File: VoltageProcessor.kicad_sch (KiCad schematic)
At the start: 29 parts, among them J1 PJ301M-12, J2 PJ301M-12, J3 Eurorack power, J3 PJ301M-12, J4 PJ301M-12, U1 TL074

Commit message: IO Placement
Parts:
- renumbered J3 to J5
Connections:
- net at R1.1: now also RV1.2
- net at RV2.2: now also R2.1
- no-connect marks 8 -> 4
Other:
- moved on the sheet: J1, J2, RV1, RV2

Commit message: Pre route
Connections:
- net GND: no longer U1.6 (-)
- net at R4.2, R6.1, R9.1: now also U1.1; no longer U1.7
- net at R1.2, R3.1: now also U1.5 (+); no longer U1.2 (-)
- net at R3.2, R5.1, R8.1: now also U1.7; no longer U1.1
- net at R2.2, R4.1: now also U1.2 (-); no longer U1.5 (+)

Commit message: Add silkscreen text, and last DRC issues
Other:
- company: (none) -> joppeboeve.nl
- title: (none) -> Voltage Processor
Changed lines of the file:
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@@
 	(generator_version "8.0")
 	(paper "A4")
+	(title_block
+		(title "Voltage Processor")
+		(date "2024-07-28")
+		(rev "0.1")
+		(company "joppeboeve.nl")
+	)
 	(junction
 		(at 113.03 177.8)

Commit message: Connected input CV jack's switch to GND instead of NC Add schematic picture
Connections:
- net GND: now also J1.2, J2.2
- no-connect marks 4 -> 2
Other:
- note removed: "NOTE: Maybe ground jacks instead of NC?"
- moved on the sheet: C1, C2, C3, C4, C5, C6, J1, J2, J3, J4, J5, R1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

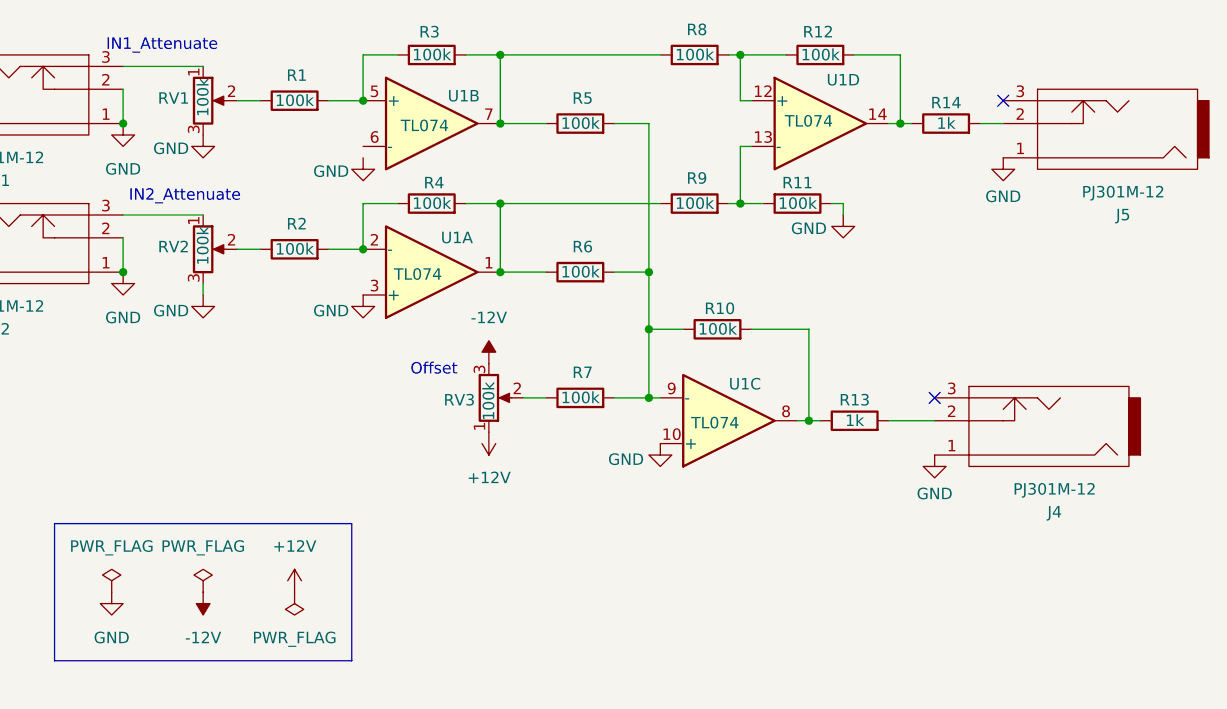
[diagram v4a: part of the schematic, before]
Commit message: Swapped `U1B` inputs to match that of `U1A`, so that it does work
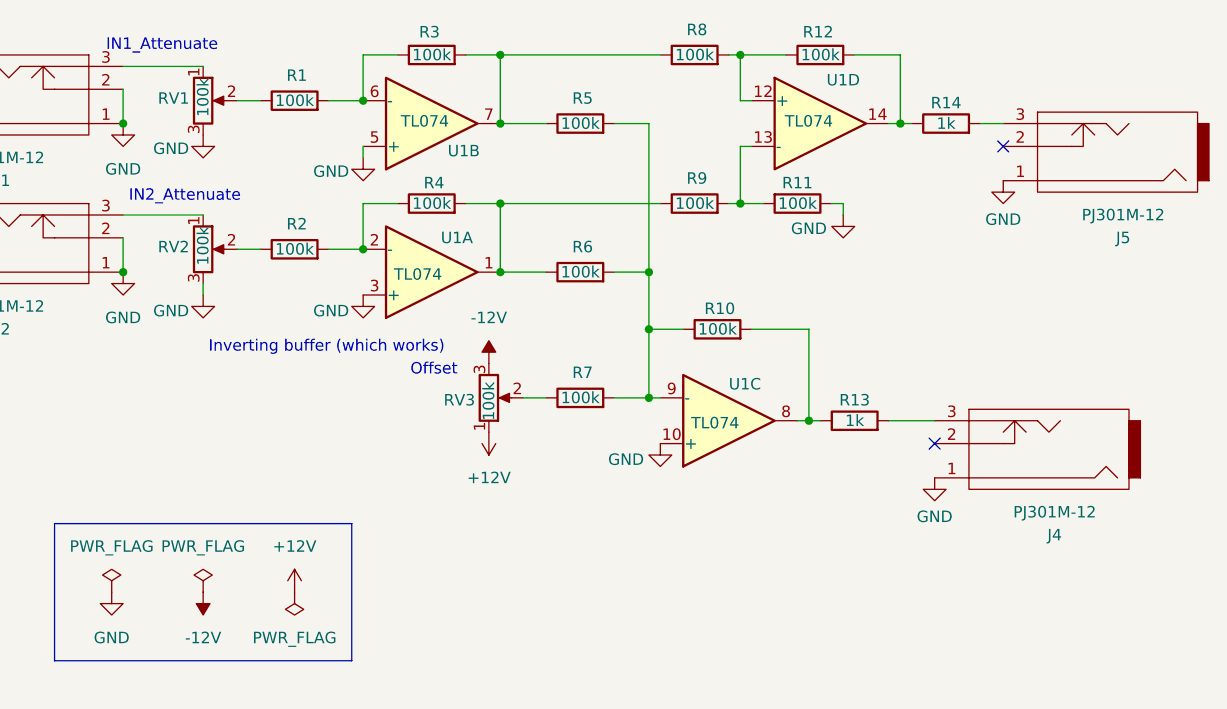
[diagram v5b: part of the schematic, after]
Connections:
- net GND: now also U1.5 (+)
- net at J4.2: no longer R13.2
- net at J4.3: now also R13.2
- net at R1.2, R3.1: now also U1.6 (-); no longer U1.5 (+)
- net at J5.2: no longer R14.2
- net at J5.3: now also R14.2
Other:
- note added: "Inverting buffer (which works)"
- moved on the sheet: J4, J5
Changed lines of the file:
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@@
 	)
 	(no_connect
-		(at 167.64 35.56)
+		(at 160.02 73.66)
 	)
 	(no_connect
-		(at 160.02 68.58)
+		(at 167.64 40.64)
 	)
 	(wire
@@
 	(wire
 		(pts
-			(xy 154.94 71.12) (xy 160.02 71.12)
-		)
-		(stroke
-			(width 0)
-			(type default)
-		)
-	)
-	(wire
-		(pts
 			(xy 138.43 40.64) (xy 138.43 46.99)
 		)
@@
 	(wire
 		(pts
-			(xy 111.76 54.61) (xy 116.84 54.61)
+			(xy 154.94 71.12) (xy 160.02 71.12)
 		)
 		(stroke
@@
 	(wire
 		(pts
-			(xy 114.3 68.58) (xy 116.84 68.58)
+			(xy 111.76 54.61) (xy 116.84 54.61)
 		)
 		(stroke
@@
 		)
 	)
-	(polyline
+	(wire
 		(pts
-			(xy 62.23 82.55) (xy 95.25 82.55)
+			(xy 114.3 68.58) (xy 116.84 68.58)
 		)
 		(stroke
@@
 		)
 	)
-	(wire
+	(polyline
 		(pts
-			(xy 165.1 38.1) (xy 167.64 38.1)
+			(xy 62.23 82.55) (xy 95.25 82.55)
 		)
 		(stroke
@@
 	(wire
 		(pts
+			(xy 96.52 40.64) (xy 96.52 41.91)
+		)
+		(stroke
+			(width 0)
+			(type default)
+		)
+	)
+	(wire
+		(pts
 			(xy 128.27 54.61) (xy 128.27 60.96)
 		)
@@
 	(wire
 		(pts
+			(xy 165.1 38.1) (xy 167.64 38.1)
+		)
+		(stroke
+			(width 0)
+			(type default)
+		)
+	)
+	(wire
+		(pts
 			(xy 36.83 83.82) (xy 34.29 83.82)
 		)
@@
 		)
 	)
+	(text "Inverting buffer (which works)"
+		(exclude_from_sim no)
+		(at 92.456 62.992 0)
+		(effects
+			(font
+				(size 1.27 1.27)
+			)
+		)
+	)
 	(text "IN2_Attenuate"
 		(exclude_from_sim no)
@@
 	(symbol
 		(lib_id "eurocad:PJ301M-12")
-		(at 171.45 71.12 180)
+		(at 171.45 73.66 180)
 		(unit 1)
 		(exclude_from_sim no)
@@
 		(dnp no)
 		(property "Reference" "J4"
-			(at 173.355 81.28 0)
+			(at 173.355 83.82 0)
 			(effects
 				(font
@@
 		)
 		(property "Value" "PJ301M-12"
-			(at 173.355 78.74 0)
+			(at 173.355 81.28 0)
 			(effects
 				(font
@@
 		)
 		(property "Footprint" "Eurocad:PJ301M-12"
-			(at 171.45 71.12 0)
+			(at 171.45 73.66 0)
 			(effects
 				(font
@@
 		)
 		(property "Datasheet" ""
-			(at 171.45 71.12 0)
+			(at 171.45 73.66 0)
 			(effects
 				(font
@@
 		)
 		(property "Description" ""
-			(at 171.45 71.12 0)
+			(at 171.45 73.66 0)
 			(effects
 				(font
@@
 	(symbol
 		(lib_id "eurocad:PJ301M-12")
-		(at 179.07 38.1 180)
+		(at 179.07 40.64 180)
 		(unit 1)
 		(exclude_from_sim no)
@@
 		(dnp no)
 		(property "Reference" "J5"
-			(at 180.975 48.26 0)
+			(at 180.975 50.8 0)
 			(effects
 				(font
@@
 		)
 		(property "Value" "PJ301M-12"
-			(at 180.975 45.72 0)
+			(at 180.975 48.26 0)
 			(effects
 				(font
@@
 		)
 		(property "Footprint" "Eurocad:PJ301M-12"
-			(at 179.07 38.1 0)
+			(at 179.07 40.64 0)
 			(effects
 				(font
@@
 		)
 		(property "Datasheet" ""
-			(at 179.07 38.1 0)
+			(at 179.07 40.64 0)
 			(effects
 				(font
@@
 		)
 		(property "Description" ""
-			(at 179.07 38.1 0)
+			(at 179.07 40.64 0)
 			(effects
 				(font
@@
 	(symbol
 		(lib_id "power:GND")
-		(at 167.64 41.91 0)
+		(at 167.64 44.45 0)
 		(unit 1)
 		(exclude_from_sim no)
@@
 		(dnp no)
 		(property "Reference" "#PWR024"
-			(at 167.64 48.26 0)
+			(at 167.64 50.8 0)
 			(effects
 				(font
@@
 		)
 		(property "Value" "GND"
-			(at 167.64 46.228 0)
+			(at 167.64 48.768 0)
 			(effects
 				(font
@@
 		)
 		(property "Footprint" ""
-			(at 167.64 41.91 0)
+			(at 167.64 44.45 0)
 			(effects
 				(font
@@
 		)
 		(property "Datasheet" ""
-			(at 167.64 41.91 0)
+			(at 167.64 44.45 0)
 			(effects
 				(font
@@
 		)
 		(property "Description" "Power symbol creates a global label with name \"GND\" , ground"
-			(at 167.64 41.91 0)
+			(at 167.64 44.45 0)
 			(effects
 				(font
@@
 		(lib_id "Amplifier_Operational:TL074")
 		(at 104.14 38.1 0)
+		(mirror x)
 		(unit 2)
 		(exclude_from_sim no)
@@
 		(dnp no)
 		(property "Reference" "U1"
-			(at 107.696 35.052 0)
+			(at 107.696 41.148 0)
 			(effects
 				(font
@@
 		)
 		(property "Value" "TL074"
-			(at 103.378 38.354 0)
+			(at 103.378 37.846 0)
 			(effects
 				(font
@@
 		)
 		(property "Footprint" "Package_DIP:DIP-14_W7.62mm"
-			(at 102.87 35.56 0)
+			(at 102.87 40.64 0)
 			(effects
 				(font
@@
 		)
 		(property "Datasheet" "http://www.ti.com/lit/ds/symlink/tl071.pdf"
-			(at 105.41 33.02 0)
+			(at 105.41 43.18 0)
 			(effects
 				(font
@@
 	(symbol
 		(lib_id "power:GND")
-		(at 160.02 74.93 0)
+		(at 160.02 77.47 0)
 		(unit 1)
 		(exclude_from_sim no)
@@
 		(dnp no)
 		(property "Reference" "#PWR023"
-			(at 160.02 81.28 0)
+			(at 160.02 83.82 0)
 			(effects
 				(font
@@
 		)
 		(property "Value" "GND"
-			(at 160.02 79.248 0)
+			(at 160.02 81.788 0)
 			(effects
 				(font
@@
 		)
 		(property "Footprint" ""
-			(at 160.02 74.93 0)
+			(at 160.02 77.47 0)
 			(effects
 				(font
@@
 		)
 		(property "Datasheet" ""
-			(at 160.02 74.93 0)
+			(at 160.02 77.47 0)
 			(effects
 				(font
@@
 		)
 		(property "Description" "Power symbol creates a global label with name \"GND\" , ground"
-			(at 160.02 74.93 0)
+			(at 160.02 77.47 0)
 			(effects
 				(font

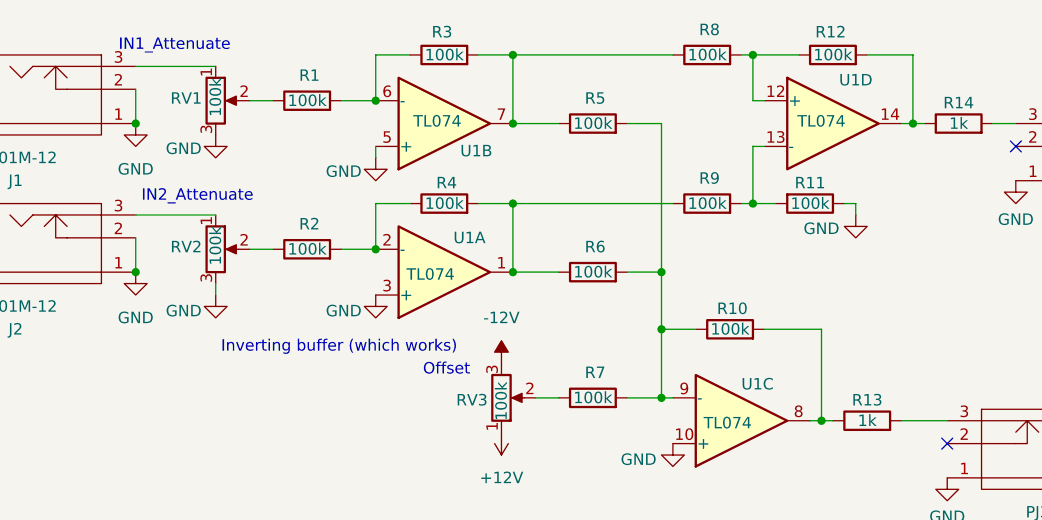
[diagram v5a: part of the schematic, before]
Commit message: Switched `RV1` and `RV2`
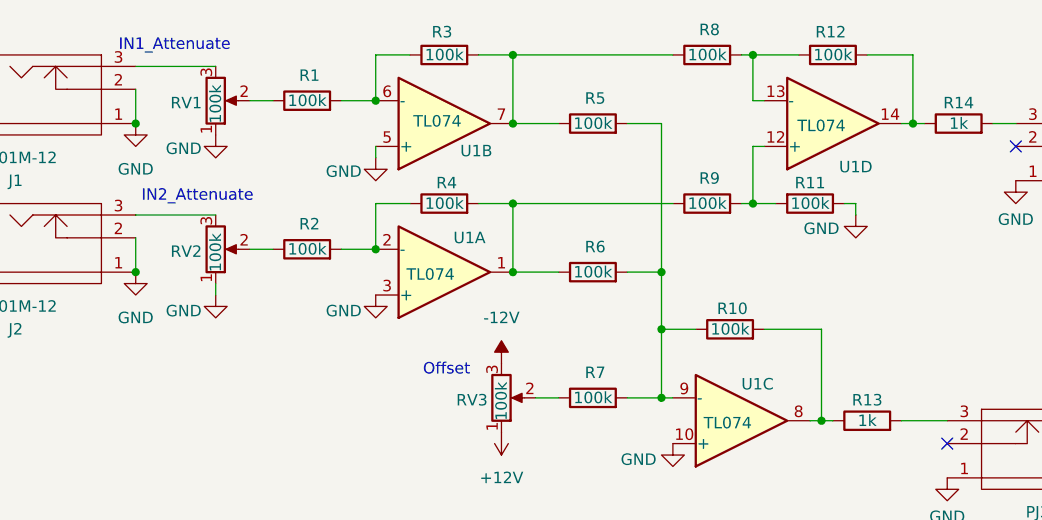
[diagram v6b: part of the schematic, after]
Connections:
- net GND: now also RV1.1, RV2.1; no longer RV1.3, RV2.3
- net at R11.2, R9.2: now also U1.12 (+); no longer U1.13 (-)
- net at J2.3: now also RV2.3; no longer RV2.1
- net at R12.1, R8.2: now also U1.13 (-); no longer U1.12 (+)
- net at J1.3: now also RV1.3; no longer RV1.1
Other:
- note removed: "Inverting buffer (which works)"
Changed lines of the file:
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@@
 		)
 	)
-	(text "Inverting buffer (which works)"
-		(exclude_from_sim no)
-		(at 92.456 62.992 0)
-		(effects
-			(font
-				(size 1.27 1.27)
-			)
-		)
-	)
 	(text "IN2_Attenuate"
 		(exclude_from_sim no)
@@
 		(lib_id "Amplifier_Operational:TL074")
 		(at 147.32 38.1 0)
+		(mirror x)
 		(unit 4)
 		(exclude_from_sim no)
@@
 		(dnp no)
 		(property "Reference" "U1"
-			(at 149.86 33.274 0)
+			(at 149.86 42.926 0)
 			(effects
 				(font
@@
 		)
 		(property "Value" "TL074"
-			(at 146.05 37.846 0)
+			(at 146.05 38.354 0)
 			(effects
 				(font
@@
 		)
 		(property "Footprint" "Package_DIP:DIP-14_W7.62mm"
-			(at 146.05 35.56 0)
+			(at 146.05 40.64 0)
 			(effects
 				(font
@@
 		)
 		(property "Datasheet" "http://www.ti.com/lit/ds/symlink/tl071.pdf"
-			(at 148.59 33.02 0)
+			(at 148.59 43.18 0)
 			(effects
 				(font
@@
 		(lib_id "Device:R_Potentiometer")
 		(at 78.74 52.07 0)
+		(mirror x)
 		(unit 1)
 		(exclude_from_sim no)
@@
 		(dnp no)
 		(property "Reference" "RV2"
-			(at 77.216 51.816 0)
+			(at 77.216 52.324 0)
 			(effects
 				(font
@@
 		)
 		(property "Value" "100k"
-			(at 78.74 49.53 90)
+			(at 78.74 54.61 90)
 			(effects
 				(font
@@
 		(lib_id "Device:R_Potentiometer")
 		(at 78.74 35.56 0)
+		(mirror x)
 		(unit 1)
 		(exclude_from_sim no)
@@
 		(dnp no)
 		(property "Reference" "RV1"
-			(at 77.216 35.306 0)
+			(at 77.216 35.814 0)
 			(effects
 				(font
@@
 		)
 		(property "Value" "100k"
-			(at 78.74 33.02 90)
+			(at 78.74 38.1 90)
 			(effects
 				(font

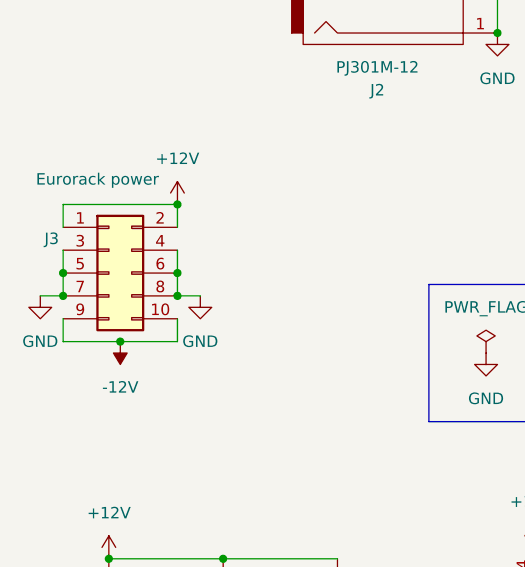
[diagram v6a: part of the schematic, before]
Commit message: Implemented fixes in schematic
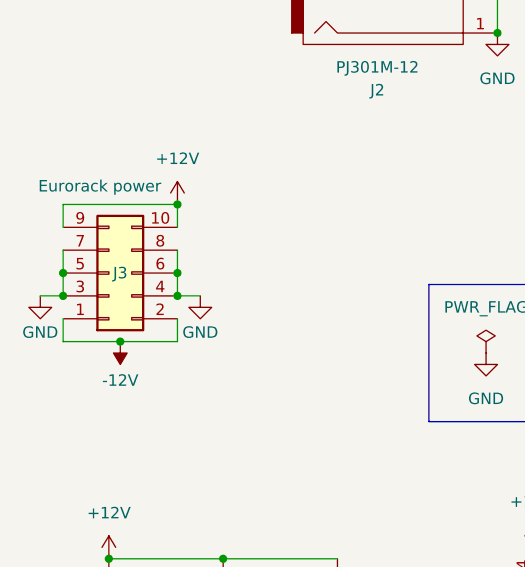
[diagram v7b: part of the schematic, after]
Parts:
- C5, C6: footprint Capacitor_THT:C_Radial_D5.0mm_H11.0mm_P2.00mm -> Capacitor_THT:CP_Radial_D5.0mm_P2.00mm
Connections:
- net +12V: now also J3.10 (Pin_10), J3.9 (Pin_9); no longer J3.1 (Pin_1), J3.2 (Pin_2)
- net -12V: now also J3.1 (Pin_1), J3.2 (Pin_2); no longer J3.10 (Pin_10), J3.9 (Pin_9)
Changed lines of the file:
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@@
 			)
 		)
-		(property "Footprint" "Capacitor_THT:C_Radial_D5.0mm_H11.0mm_P2.00mm"
+		(property "Footprint" "Capacitor_THT:CP_Radial_D5.0mm_P2.00mm"
 			(at 53.0352 128.27 0)
 			(effects
@@
 		(on_board yes)
 		(dnp no)
-		(fields_autoplaced yes)
 		(property "Reference" "#PWR010"
 			(at 19.05 90.17 0)
@@
 		)
 		(property "Value" "GND"
-			(at 19.05 88.9 0)
+			(at 19.05 87.884 0)
 			(effects
 				(font
@@
 		(on_board yes)
 		(dnp no)
-		(fields_autoplaced yes)
 		(property "Reference" "#PWR017"
 			(at 36.83 90.17 0)
@@
 		)
 		(property "Value" "GND"
-			(at 36.83 88.9 0)
+			(at 36.83 87.884 0)
 			(effects
 				(font
@@
 		(lib_id "Connector_Generic:Conn_02x05_Odd_Even")
 		(at 26.67 81.28 0)
+		(mirror x)
 		(unit 1)
 		(exclude_from_sim no)
@@
 		(dnp no)
 		(property "Reference" "J3"
-			(at 20.32 77.47 0)
+			(at 27.94 81.28 0)
 			(effects
 				(font
@@
 		)
 		(property "Value" "Eurorack power"
-			(at 25.4 70.866 0)
+			(at 25.654 71.628 0)
 			(effects
 				(font
@@
 			)
 		)
-		(property "Footprint" "Capacitor_THT:C_Radial_D5.0mm_H11.0mm_P2.00mm"
+		(property "Footprint" "Capacitor_THT:CP_Radial_D5.0mm_P2.00mm"
 			(at 53.0352 120.65 0)
 			(effects
@@
 		(on_board yes)
 		(dnp no)
-		(fields_autoplaced yes)
 		(property "Reference" "#PWR013"
 			(at 27.94 85.09 0)
@@
 		)
 		(property "Value" "-12V"
-			(at 27.94 93.98 0)
-			(effects
-				(font
+			(at 27.94 93.218 0)
+			(effects
+				(font
